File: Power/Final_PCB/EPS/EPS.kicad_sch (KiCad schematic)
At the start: 0 parts

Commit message: Completed EPS Board
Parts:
- added BT1: Main_Bat, Connector_PinHeader_2.54mm:PinHeader_1x02_P2.54mm_Vertical, symbol Device:Battery_Cell
- added BT2: Backup_Cell, Battery:BatteryHolder_Multicomp_BC-2001_1x2032, symbol Device:Battery_Cell
- added C1, C2, C3, C4: 470uF, Capacitor_THT:CP_Radial_D8.0mm_P3.50mm, symbol Device:C_Polarized
- added D1: D, Diode_THT:D_DO-15_P10.16mm_Horizontal, symbol Device:D
- added D2, D3, D4, D5: LED, LED_THT:LED_D3.0mm, symbol Device:LED
- added F1, F2, F3, F4, F5, F6, F7: Fuse, Fuse:Fuse_Blade_Mini_directSolder, symbol Device:Fuse
- added J1: Left_Header, Connector_PinHeader_2.54mm:PinHeader_2x25_P2.54mm_Vertical, symbol Connector_Generic:Conn_02x25_Counter_Clockwise
- added J2: Right_Header, Connector_PinHeader_2.54mm:PinHeader_2x25_P2.54mm_Vertical, symbol Connector_Generic:Conn_02x25_Counter_Clockwise
- added R1: 2.7K, Resistor_THT:R_Axial_DIN0207_L6.3mm_D2.5mm_P7.62mm_Horizontal, symbol Device:R
- added R2: 1.5K, Resistor_THT:R_Axial_DIN0207_L6.3mm_D2.5mm_P7.62mm_Horizontal, symbol Device:R
- added R3: 1K, Resistor_THT:R_Axial_DIN0207_L6.3mm_D2.5mm_P7.62mm_Horizontal, symbol Device:R
- added R4: 330, Resistor_THT:R_Axial_DIN0207_L6.3mm_D2.5mm_P7.62mm_Horizontal, symbol Device:R
- added TP1, TP2, TP3, TP4: TestPoint, TestPoint:TestPoint_Loop_D2.50mm_Drill1.0mm, symbol Connector:TestPoint
- added U1: INA226, INA226_Breakout:INA_Breakout, symbol Sensor_Energy:INA226
- added U2: MT3608-28, MT3608_Breakout:MODULE_MT3608_DC-DC_STEP_UP_CONVERTER_2A_BOOSTER_MODULE, symbol MT3608_Breakout:MT3608_DC-DC_STEP_UP_CONVERTER_2A_BOOSTER_MODULE
- added U3: LM2596S-5, LM2596S_Breakout:LM2596_Breakout, symbol MT3608_Breakout:MT3608_DC-DC_STEP_UP_CONVERTER_2A_BOOSTER_MODULE
- added U4: LM2596S-3.3, LM2596S_Breakout:LM2596_Breakout, symbol MT3608_Breakout:MT3608_DC-DC_STEP_UP_CONVERTER_2A_BOOSTER_MODULE
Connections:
- new net: BT1.1 (+), C1.1, F1.1, TP1.1
- new net: F2.2, U4.VIN_P (VIN+)
- new net: F3.1, U4.VOUT_P (VOUT+)
- new net: D4.2 (A), R3.2
- new net: BT2.2 (-), D1.2 (A)
- new net: F6.2, U2.VIN_P (VIN+)
- new net: F4.2, U3.VIN_P (VIN+)
- new net: F5.1, U3.VOUT_P (VOUT+)
- new net: F7.1, U2.VOUT_P (VOUT+)
- new net: D3.2 (A), R2.2
- new net: D5.2 (A), R4.2
- new net: D2.2 (A), R1.2
- new net 14.8V: F2.1, F4.1, F6.1, J1.13 (Pin_13), J1.14 (Pin_14), J1.15 (Pin_15), J1.16 (Pin_16), J2.13 (Pin_13), J2.14 (Pin_14), J2.15 (Pin_15), J2.16 (Pin_16), R2.1, U1.9 (Vin-)
- new net 28V: C4.1, F7.2, J1.17 (Pin_17), J1.18 (Pin_18), J1.19 (Pin_19), J1.20 (Pin_20), J2.17 (Pin_17), J2.18 (Pin_18), J2.19 (Pin_19), J2.20 (Pin_20), R1.1, TP4.1
- new net 3V3: C2.1, F3.2, J1.5 (Pin_5), J1.6 (Pin_6), J1.7 (Pin_7), J1.8 (Pin_8), J2.5 (Pin_5), J2.6 (Pin_6), J2.7 (Pin_7), J2.8 (Pin_8), R4.1, TP2.1, U1.6 (VS)
- new net 5V: C3.1, F5.2, J1.10 (Pin_10), J1.11 (Pin_11), J1.12 (Pin_12), J1.9 (Pin_9), J2.10 (Pin_10), J2.11 (Pin_11), J2.12 (Pin_12), J2.9 (Pin_9), R3.1, TP3.1
- new net GND: BT1.2 (-), C1.2, C2.2, C3.2, C4.2, D1.1 (K), D2.1 (K), D3.1 (K), D4.1 (K), D5.1 (K), J1.1 (Pin_1), J1.2 (Pin_2), J1.3 (Pin_3), J1.4 (Pin_4), J1.45 (Pin_45), J1.46 (Pin_46), J1.47 (Pin_47), J1.48 (Pin_48), J1.49 (Pin_49), J1.50 (Pin_50), J2.1 (Pin_1), J2.2 (Pin_2), J2.3 (Pin_3), J2.4 (Pin_4), J2.45 (Pin_45), J2.46 (Pin_46), J2.47 (Pin_47), J2.48 (Pin_48), J2.49 (Pin_49), J2.50 (Pin_50), U1.7 (GND), U2.VIN_N (VIN-), U2.VOUT_N (VOUT-), U3.VIN_N (VIN-), U3.VOUT_N (VOUT-), U4.VIN_N (VIN-), U4.VOUT_N (VOUT-)
- new net INA_14.8V: F1.2, U1.10 (Vin+), U1.8 (Vbus)
- new net INA_ALERT: J1.25 (Pin_25), J2.25 (Pin_25), U1.3 (~{Alert})
- new net SCL: J1.23 (Pin_23), J2.23 (Pin_23), U1.5 (SCL)
- new net SDA: J1.24 (Pin_24), J2.24 (Pin_24), U1.4 (SDA)
- new net VBAT: BT2.1 (+), J1.21 (Pin_21), J1.22 (Pin_22), J2.21 (Pin_21), J2.22 (Pin_22)
- no-connect marks 0 -> 40
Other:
- note added: "Batteries"
- note added: "Interboard Headers"
- note added: "Monitoring LEDs"
- note added: "Voltage Converters"
- note added: "Voltage/Current Monitor"
- title: (none) -> HYPERIONyX - Electrical Power System Board

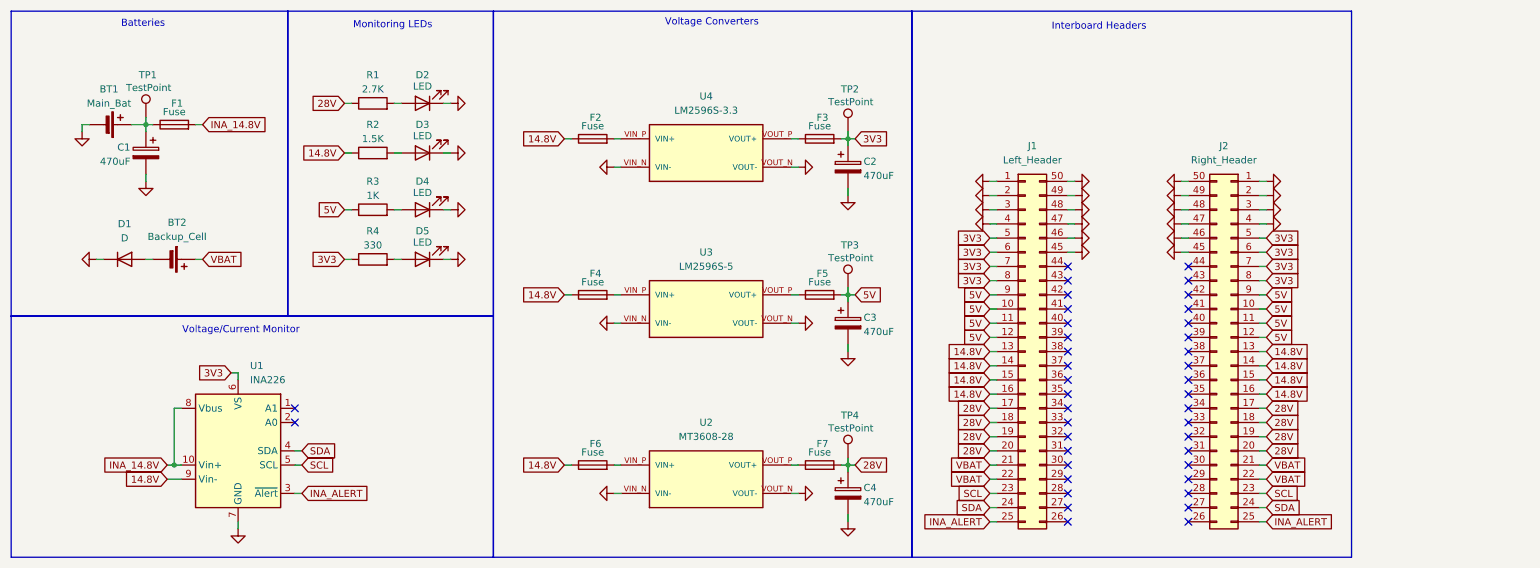
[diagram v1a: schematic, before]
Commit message: Finalised EPS tracks/connections
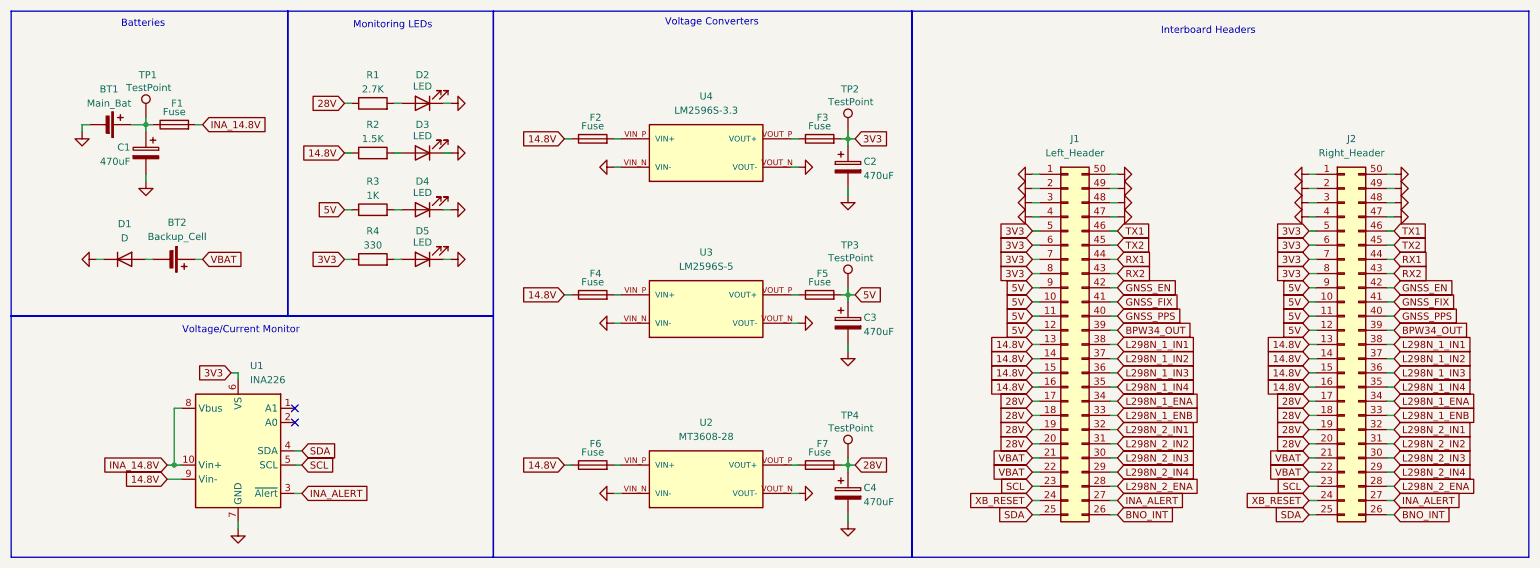
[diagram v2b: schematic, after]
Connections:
- net GND: no longer J1.45 (Pin_45), J1.46 (Pin_46), J2.45 (Pin_45), J2.46 (Pin_46)
- net INA_ALERT: now also J1.27 (Pin_27), J2.27 (Pin_27); no longer J1.25 (Pin_25), J2.25 (Pin_25)
- net SDA: now also J1.25 (Pin_25), J2.25 (Pin_25); no longer J1.24 (Pin_24), J2.24 (Pin_24)
- net BNO_INT: now reaches J1.26 (Pin_26)
- net BNO_INT: now also J2.26 (Pin_26)
- net L298N_2_ENA: now reaches J1.28 (Pin_28)
- net L298N_2_ENA: now also J2.28 (Pin_28)
- net L298N_2_IN4: now reaches J1.29 (Pin_29)
- net L298N_2_IN4: now also J2.29 (Pin_29)
- net L298N_2_IN3: now reaches J1.30 (Pin_30)
- net L298N_2_IN3: now also J2.30 (Pin_30)
- net L298N_2_IN2: now reaches J1.31 (Pin_31)
- net L298N_2_IN2: now also J2.31 (Pin_31)
- net L298N_2_IN1: now reaches J1.32 (Pin_32)
- net L298N_2_IN1: now also J2.32 (Pin_32)
- net L298N_1_ENB: now reaches J1.33 (Pin_33)
- net L298N_1_ENB: now also J2.33 (Pin_33)
- net L298N_1_ENA: now reaches J1.34 (Pin_34)
- net L298N_1_ENA: now also J2.34 (Pin_34)
- net L298N_1_IN4: now reaches J1.35 (Pin_35)
- net L298N_1_IN4: now also J2.35 (Pin_35)
- net L298N_1_IN3: now reaches J1.36 (Pin_36)
- net L298N_1_IN3: now also J2.36 (Pin_36)
- net L298N_1_IN2: now reaches J1.37 (Pin_37)
- net L298N_1_IN2: now also J2.37 (Pin_37)
- net L298N_1_IN1: now reaches J1.38 (Pin_38)
- net L298N_1_IN1: now also J2.38 (Pin_38)
- net BPW34_OUT: now reaches J1.39 (Pin_39)
- net BPW34_OUT: now also J2.39 (Pin_39)
- net GNSS_PPS: now reaches J1.40 (Pin_40)
- net GNSS_PPS: now also J2.40 (Pin_40)
- net GNSS_FIX: now reaches J1.41 (Pin_41)
- net GNSS_FIX: now also J2.41 (Pin_41)
- net GNSS_EN: now reaches J1.42 (Pin_42)
- net GNSS_EN: now also J2.42 (Pin_42)
- net RX2: now reaches J1.43 (Pin_43)
- net RX2: now also J2.43 (Pin_43)
- net RX1: now reaches J1.44 (Pin_44)
- net RX1: now also J2.44 (Pin_44)
- new net TX1: J1.46 (Pin_46), J2.46 (Pin_46)
- new net TX2: J1.45 (Pin_45), J2.45 (Pin_45)
- new net XB_RESET: J1.24 (Pin_24), J2.24 (Pin_24)
- no-connect marks 40 -> 2
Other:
- moved on the sheet: J1

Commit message: Fixed EPS board to have 12V instead of 28V rail
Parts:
- added TP5: TestPoint, TestPoint:TestPoint_Loop_D2.50mm_Drill1.0mm, symbol Connector:TestPoint
- R1: value 2.7K -> 1.5K
- R2: value 1.5K -> 1K
- R3: value 1K -> 330
- R4: value 330 -> 150
- U2: value MT3608-28 -> LM2596-12; footprint MT3608_Breakout:MODULE_MT3608_DC-DC_STEP_UP_CONVERTER_2A_BOOSTER_MODULE -> LM2596S_Breakout:LM2596_Breakout
- renumbered D2 to D1, D3 to D2, D4 to D3, D5 to D4, D1 to D5, TP4 to TP2, TP2 to TP4
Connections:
- net 14.8V: now also R1.1; no longer R2.1
- net VBAT: now also TP5.1
- net 28V renamed 12V
- net 12V: now also R2.1; no longer R1.1
- net L298N_2_IN3: no longer names the net of J1.30 (Pin_30)
- net L298N_2_IN3: no longer J2.30 (Pin_30)
- net L298N_2_IN4: no longer names the net of J1.29 (Pin_29)
- net L298N_2_IN4: no longer J2.29 (Pin_29)
- no-connect marks 2 -> 4

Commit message: Revert EPS schematic and PCB to version with MT3608 boost converter
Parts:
- removed TP5: TestPoint, TestPoint:TestPoint_Loop_D2.50mm_Drill1.0mm, symbol Connector:TestPoint
- R1: value 1.5K -> 2.7K
- R2: value 1K -> 1.5K
- R3: value 330 -> 1K
- R4: value 150 -> 330
- U2: value LM2596-12 -> MT3608-28; footprint LM2596S_Breakout:LM2596_Breakout -> MT3608_Breakout:MODULE_MT3608_DC-DC_STEP_UP_CONVERTER_2A_BOOSTER_MODULE
- renumbered D5 to D1, D1 to D2, D2 to D3, D3 to D4, D4 to D5, TP4 to TP2, TP2 to TP4
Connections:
- net 14.8V: now also R2.1; no longer R1.1
- net L298N_2_IN4: now reaches J1.29 (Pin_29)
- net L298N_2_IN4: now also J2.29 (Pin_29)
- net L298N_2_IN3: now reaches J1.30 (Pin_30)
- net L298N_2_IN3: now also J2.30 (Pin_30)
- net 12V renamed 28V
- net 28V: now also R1.1; no longer R2.1
- no-connect marks 4 -> 2

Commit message: Transitioned to ADCS-free version for worst case manufacturing scenario
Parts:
- added TP5: TestPoint, TestPoint:TestPoint_Loop_D2.50mm_Drill1.0mm, symbol Connector:TestPoint
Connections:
- net VBAT: now also TP5.1
- net L298N_1_ENA: no longer names the net of J1.34 (Pin_34)
- net L298N_1_ENA: no longer J2.34 (Pin_34)
- net L298N_1_ENB: no longer names the net of J1.33 (Pin_33)
- net L298N_1_ENB: no longer J2.33 (Pin_33)
- net L298N_1_IN1: no longer names the net of J1.38 (Pin_38)
- net L298N_1_IN1: no longer J2.38 (Pin_38)
- net L298N_1_IN2: no longer names the net of J1.37 (Pin_37)
- net L298N_1_IN2: no longer J2.37 (Pin_37)
- net L298N_1_IN3: no longer names the net of J1.36 (Pin_36)
- net L298N_1_IN3: no longer J2.36 (Pin_36)
- net L298N_1_IN4: no longer names the net of J1.35 (Pin_35)
- net L298N_1_IN4: no longer J2.35 (Pin_35)
- net L298N_2_ENA: no longer names the net of J1.28 (Pin_28)
- net L298N_2_ENA: no longer J2.28 (Pin_28)
- net L298N_2_IN1: no longer names the net of J1.32 (Pin_32)
- net L298N_2_IN1: no longer J2.32 (Pin_32)
- net L298N_2_IN2: no longer names the net of J1.31 (Pin_31)
- net L298N_2_IN2: no longer J2.31 (Pin_31)
- net L298N_2_IN3: no longer names the net of J1.30 (Pin_30)
- net L298N_2_IN3: no longer J2.30 (Pin_30)
- net L298N_2_IN4: no longer names the net of J1.29 (Pin_29)
- net L298N_2_IN4: no longer J2.29 (Pin_29)
- no-connect marks 2 -> 22

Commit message: Finalising Sensors Schematic
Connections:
- net MICROFC: now reaches J1.28 (Pin_28)
- net MICROFC: now also J2.28 (Pin_28)
- net S1223: now reaches J1.29 (Pin_29)
- net S1223: now also J2.29 (Pin_29)
- net BNO_RST: now reaches J1.30 (Pin_30)
- net BNO_RST: now also J2.30 (Pin_30)
- no-connect marks 22 -> 16
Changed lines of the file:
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@@
 	)
 	(no_connect
-		(at 259.08 95.25)
-	)
-	(no_connect
 		(at 259.08 85.09)
 	)
@@
 	)
 	(no_connect
-		(at 209.55 97.79)
-	)
-	(no_connect
 		(at 209.55 72.39)
 	)
@@
 	)
 	(no_connect
-		(at 209.55 95.25)
-	)
-	(no_connect
 		(at 259.08 74.93)
 	)
 	(no_connect
-		(at 259.08 97.79)
-	)
-	(no_connect
 		(at 209.55 90.17)
 	)
 	(no_connect
-		(at 259.08 92.71)
-	)
-	(no_connect
 		(at 259.08 90.17)
 	)
@@
 	)
 	(no_connect
-		(at 209.55 92.71)
-	)
-	(no_connect
 		(at 259.08 80.01)
 	)
@@
 	(wire
 		(pts
+			(xy 259.08 92.71) (xy 260.35 92.71)
+		)
+		(stroke
+			(width 0)
+			(type default)
+		)
+	)
+	(wire
+		(pts
 			(xy 210.82 62.23) (xy 209.55 62.23)
 		)
@@
 	(wire
 		(pts
+			(xy 209.55 95.25) (xy 210.82 95.25)
+		)
+		(stroke
+			(width 0)
+			(type default)
+		)
+	)
+	(wire
+		(pts
 			(xy 210.82 54.61) (xy 209.55 54.61)
 		)
@@
 	(wire
 		(pts
+			(xy 259.08 97.79) (xy 260.35 97.79)
+		)
+		(stroke
+			(width 0)
+			(type default)
+		)
+	)
+	(wire
+		(pts
 			(xy 162.56 34.29) (xy 162.56 35.56)
 		)
@@
 	(wire
 		(pts
+			(xy 209.55 92.71) (xy 210.82 92.71)
+		)
+		(stroke
+			(width 0)
+			(type default)
+		)
+	)
+	(wire
+		(pts
 			(xy 195.58 74.93) (xy 196.85 74.93)
 		)
@@
 	(wire
 		(pts
+			(xy 259.08 95.25) (xy 260.35 95.25)
+		)
+		(stroke
+			(width 0)
+			(type default)
+		)
+	)
+	(wire
+		(pts
 			(xy 111.76 63.5) (xy 113.03 63.5)
 		)
@@
 	(wire
 		(pts
+			(xy 209.55 97.79) (xy 210.82 97.79)
+		)
+		(stroke
+			(width 0)
+			(type default)
+		)
+	)
+	(wire
+		(pts
 			(xy 152.4 93.98) (xy 153.67 93.98)
 		)
@@
 		)
 	)
+	(global_label "MICROFC"
+		(shape input)
+		(at 260.35 97.79 0)
+		(fields_autoplaced yes)
+		(effects
+			(font
+				(size 1.27 1.27)
+			)
+			(justify left)
+		)
+		(property "Intersheetrefs" "${INTERSHEET_REFS}"
+			(at 271.6205 97.79 0)
+			(hide yes)
+			(show_name no)
+			(do_not_autoplace no)
+			(effects
+				(font
+					(size 1.27 1.27)
+				)
+				(justify left)
+			)
+		)
+	)
 	(global_label "TX2"
 		(shape input)
@@
 		)
 	)
+	(global_label "S1223"
+		(shape input)
+		(at 210.82 95.25 0)
+		(fields_autoplaced yes)
+		(effects
+			(font
+				(size 1.27 1.27)
+			)
+			(justify left)
+		)
+		(property "Intersheetrefs" "${INTERSHEET_REFS}"
+			(at 219.8527 95.25 0)
+			(hide yes)
+			(show_name no)
+			(do_not_autoplace no)
+			(effects
+				(font
+					(size 1.27 1.27)
+				)
+				(justify left)
+			)
+		)
+	)
 	(global_label "GNSS_FIX"
 		(shape input)
@@
 		)
 	)
+	(global_label "BNO_RST"
+		(shape input)
+		(at 210.82 92.71 0)
+		(fields_autoplaced yes)
+		(effects
+			(font
+				(size 1.27 1.27)
+			)
+			(justify left)
+		)
+		(property "Intersheetrefs" "${INTERSHEET_REFS}"
+			(at 222.1509 92.71 0)
+			(hide yes)
+			(show_name no)
+			(do_not_autoplace no)
+			(effects
+				(font
+					(size 1.27 1.27)
+				)
+				(justify left)
+			)
+		)
+	)
 	(global_label "VBAT"
 		(shape input)
@@
 		)
 	)
+	(global_label "MICROFC"
+		(shape input)
+		(at 210.82 97.79 0)
+		(fields_autoplaced yes)
+		(effects
+			(font
+				(size 1.27 1.27)
+			)
+			(justify left)
+		)
+		(property "Intersheetrefs" "${INTERSHEET_REFS}"
+			(at 222.0905 97.79 0)
+			(hide yes)
+			(show_name no)
+			(do_not_autoplace no)
+			(effects
+				(font
+					(size 1.27 1.27)
+				)
+				(justify left)
+			)
+		)
+	)
 	(global_label "14.8V"
 		(shape input)
@@
 		)
 	)
+	(global_label "BNO_RST"
+		(shape input)
+		(at 260.35 92.71 0)
+		(fields_autoplaced yes)
+		(effects
+			(font
+				(size 1.27 1.27)
+			)
+			(justify left)
+		)
+		(property "Intersheetrefs" "${INTERSHEET_REFS}"
+			(at 271.6809 92.71 0)
+			(hide yes)
+			(show_name no)
+			(do_not_autoplace no)
+			(effects
+				(font
+					(size 1.27 1.27)
+				)
+				(justify left)
+			)
+		)
+	)
 	(global_label "INA_14.8V"
 		(shape input)
@@
 			)
 		)
+	)
+	(global_label "S1223"
+		(shape input)
+		(at 260.35 95.25 0)
+		(fields_autoplaced yes)
+		(effects
+			(font
+				(size 1.27 1.27)
+			)
+			(justify left)
+		)
+		(property "Intersheetrefs" "${INTERSHEET_REFS}"
+			(at 269.3827 95.25 0)
+			(hide yes)
+			(show_name no)
+			(do_not_autoplace no)
+			(effects
+				(font
+					(size 1.27 1.27)
+				)
+				(justify left)
+			)
+		)

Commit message: Finalised Sensors PCB
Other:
- moved on the sheet: C1
